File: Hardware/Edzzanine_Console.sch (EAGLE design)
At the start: 32 parts, among them U1 MIC5219 3.3V, U2 FTS31XS-U

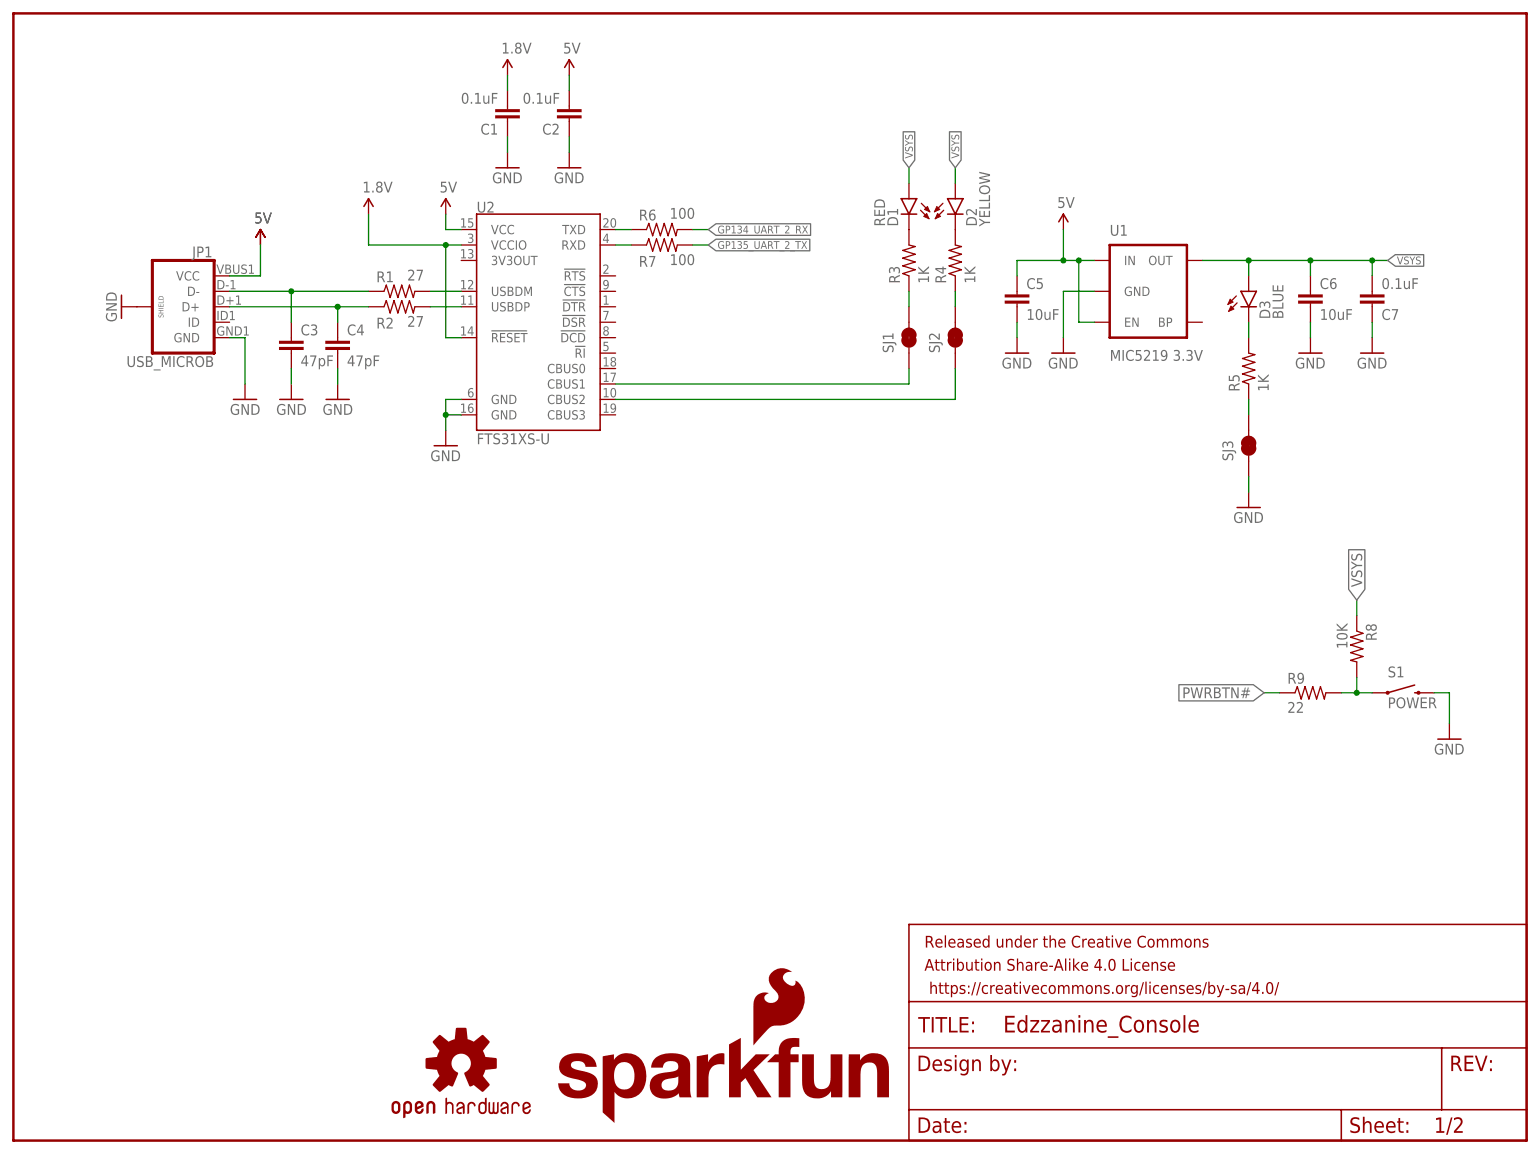
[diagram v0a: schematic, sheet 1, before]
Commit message: replaced power supply with something more powerful. added fiducials
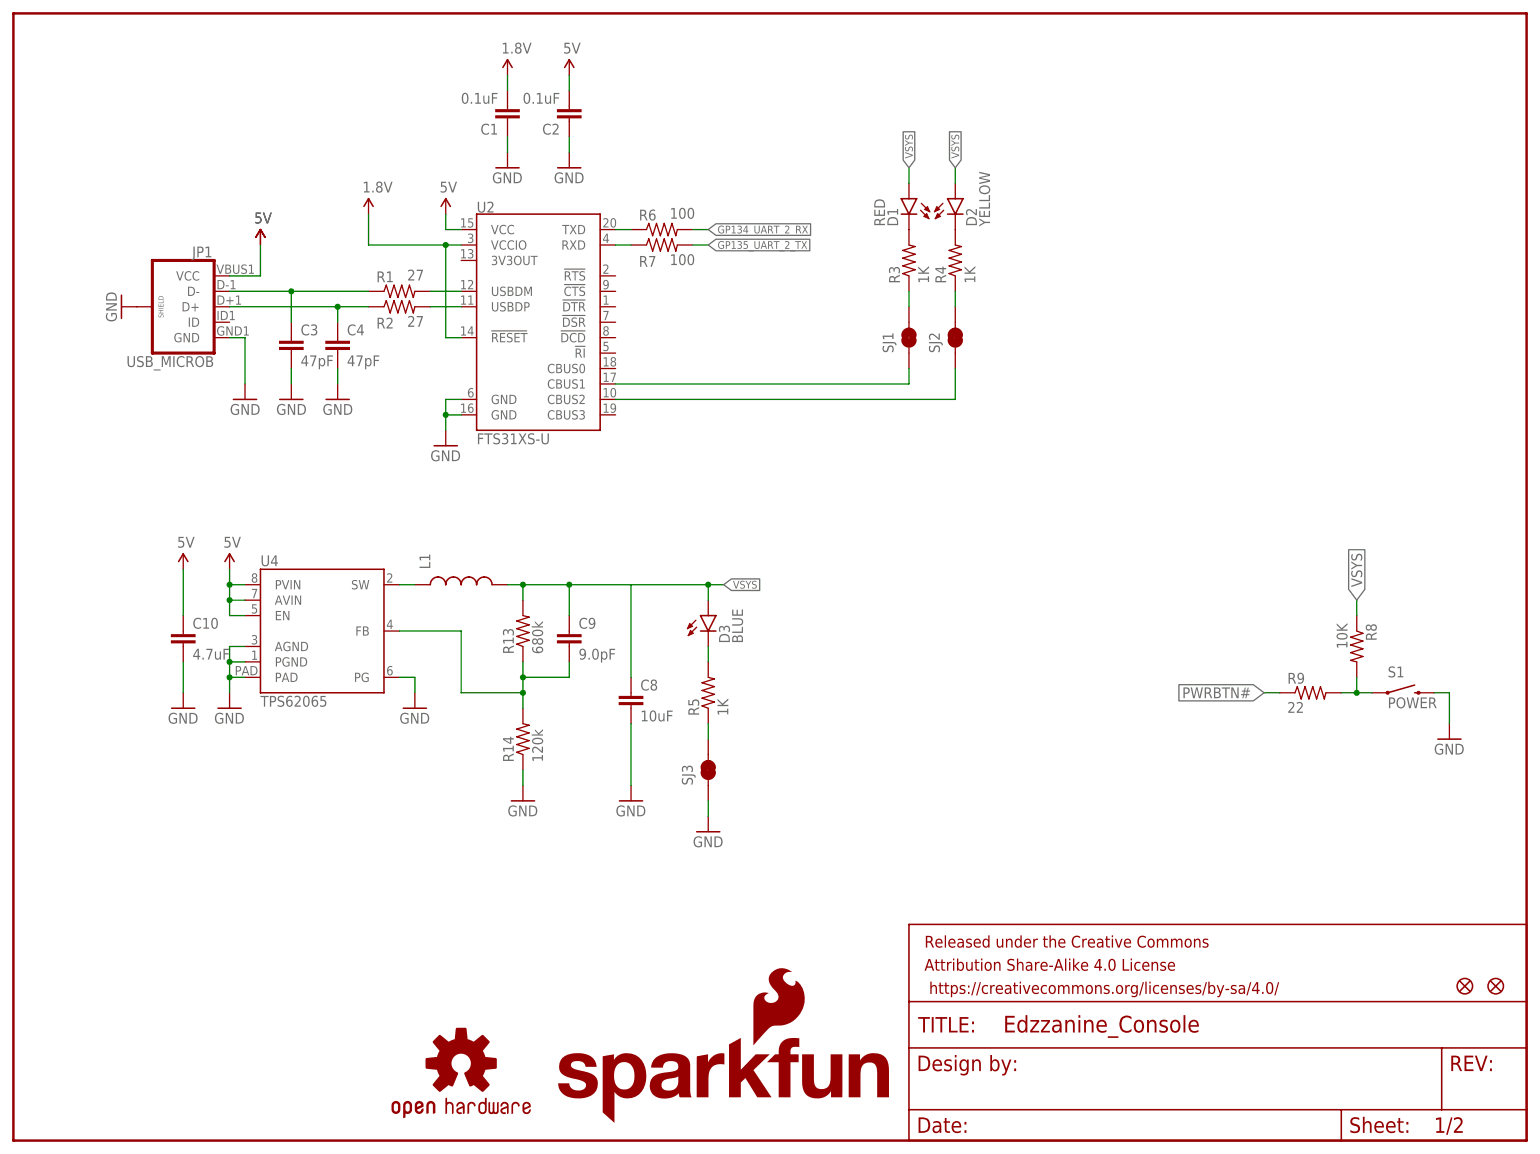
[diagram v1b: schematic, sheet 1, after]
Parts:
- removed C5, C6: 10uF, SparkFun-Capacitors:10UF-6.3V-20%(1206)
- removed C7: 0.1uF, SparkFun-Capacitors:0.1UF-25V-5%(0603)
- removed U1: MIC5219 3.3V, SparkFun-PowerIC:V_REG_MIC52193.3V
- added C10: 4.7uF, SparkFun-Capacitors:4.7UF-6.3V-10%(0603)0603
- added C8: 10uF, SparkFun-Capacitors:10UF-6.3V-20%(1206)
- added C9: 9.0pF, SparkFun-Capacitors:9.0PF-50V-10%(0603)
- added FID1, FID2: FIDUCIAL1X2, SparkFun-Aesthetics:FIDUCIAL1X2
- added L1: (no value), SparkFun-Passives:INDUCTOR
- added R13: 680k, SparkFun-Resistors:RESISTOR0603
- added R14: 120k, SparkFun-Resistors:RESISTOR0603
- added U4: TPS62065, Testing:TPS62065
- renumbered LOGO2 to LOGO4, LOGO3 to LOGO1
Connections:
- new net N$18: C9.2, R13.1, R14.2, U4.FB
- new net N$19: L1.1, U4.SW
- net 5V: now also C10.1, U4.AVIN, U4.EN, U4.PVIN; no longer C5.1, U1.EN, U1.IN
- net GND: now also C10.2, C8.2, R14.1, U4.AGND, U4.PAD, U4.PG, U4.PGND; no longer C5.2, C6.2, C7.1, U1.GND
- net VSYS: now also C8.1, C9.1, L1.2, R13.2; no longer C6.1, C7.2, U1.OUT
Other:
- moved on the sheet: D3, R5, SJ3

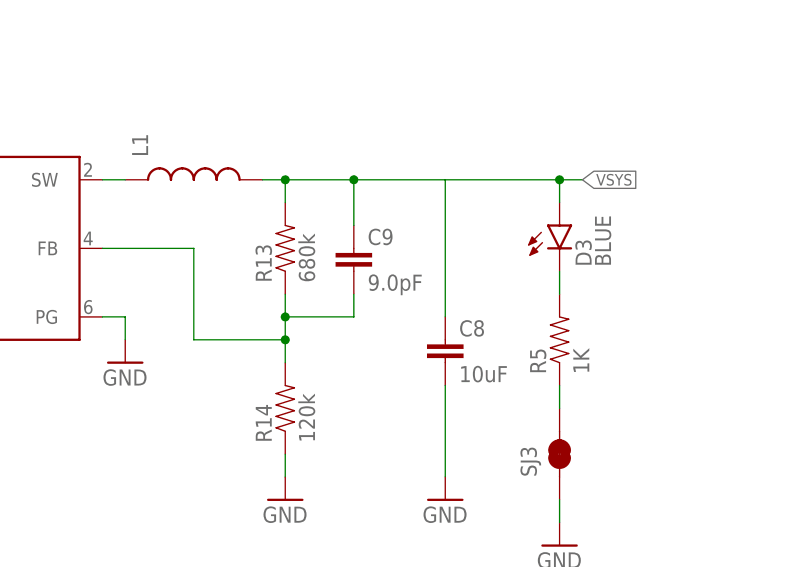
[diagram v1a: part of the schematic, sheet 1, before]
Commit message: changes to cap value
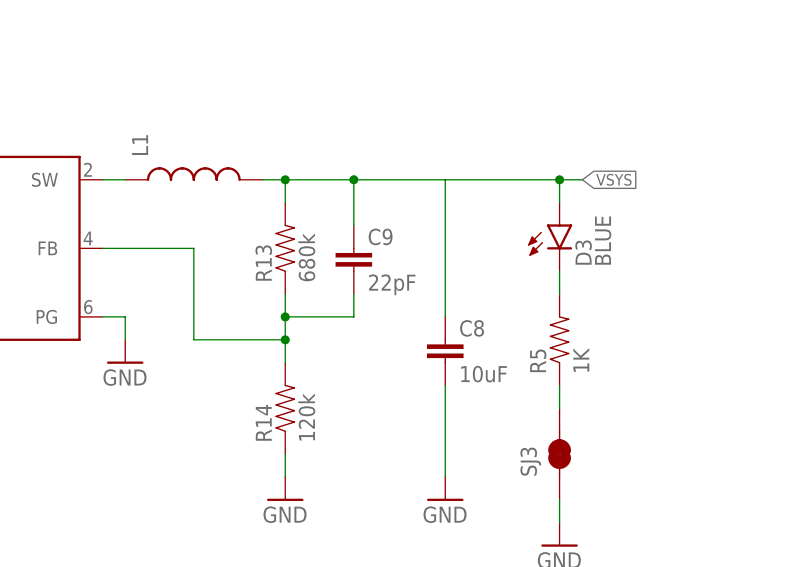
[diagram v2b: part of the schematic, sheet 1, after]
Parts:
- C9: value 9.0pF -> 22pF; device SparkFun-Capacitors:9.0PF-50V-10%(0603) -> SparkFun-Capacitors:22PF-50V-5%(0603)
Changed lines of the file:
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@@
 <part name="R13" library="SparkFun-Resistors" deviceset="RESISTOR" device="0603" value="680k"/>
 <part name="R14" library="SparkFun-Resistors" deviceset="RESISTOR" device="0603" value="120k"/>
-<part name="C9" library="SparkFun-Capacitors" deviceset="9.0PF-50V-10%(0603)" device="" value="9.0pF"/>
+<part name="C9" library="SparkFun-Capacitors" deviceset="22PF-50V-5%(0603)" device="" value="22pF"/>
 <part name="C10" library="SparkFun-Capacitors" deviceset="4.7UF-6.3V-10%(0603)" device="0603" value="4.7uF"/>
 <part name="GND19" library="SparkFun-Aesthetics" deviceset="GND" device=""/>
